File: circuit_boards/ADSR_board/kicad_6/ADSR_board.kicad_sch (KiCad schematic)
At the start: 14 parts, among them J1 ribbon_port, J2 modosc_port, J3 VCO_port, J4 VCF_port, U101 TL072

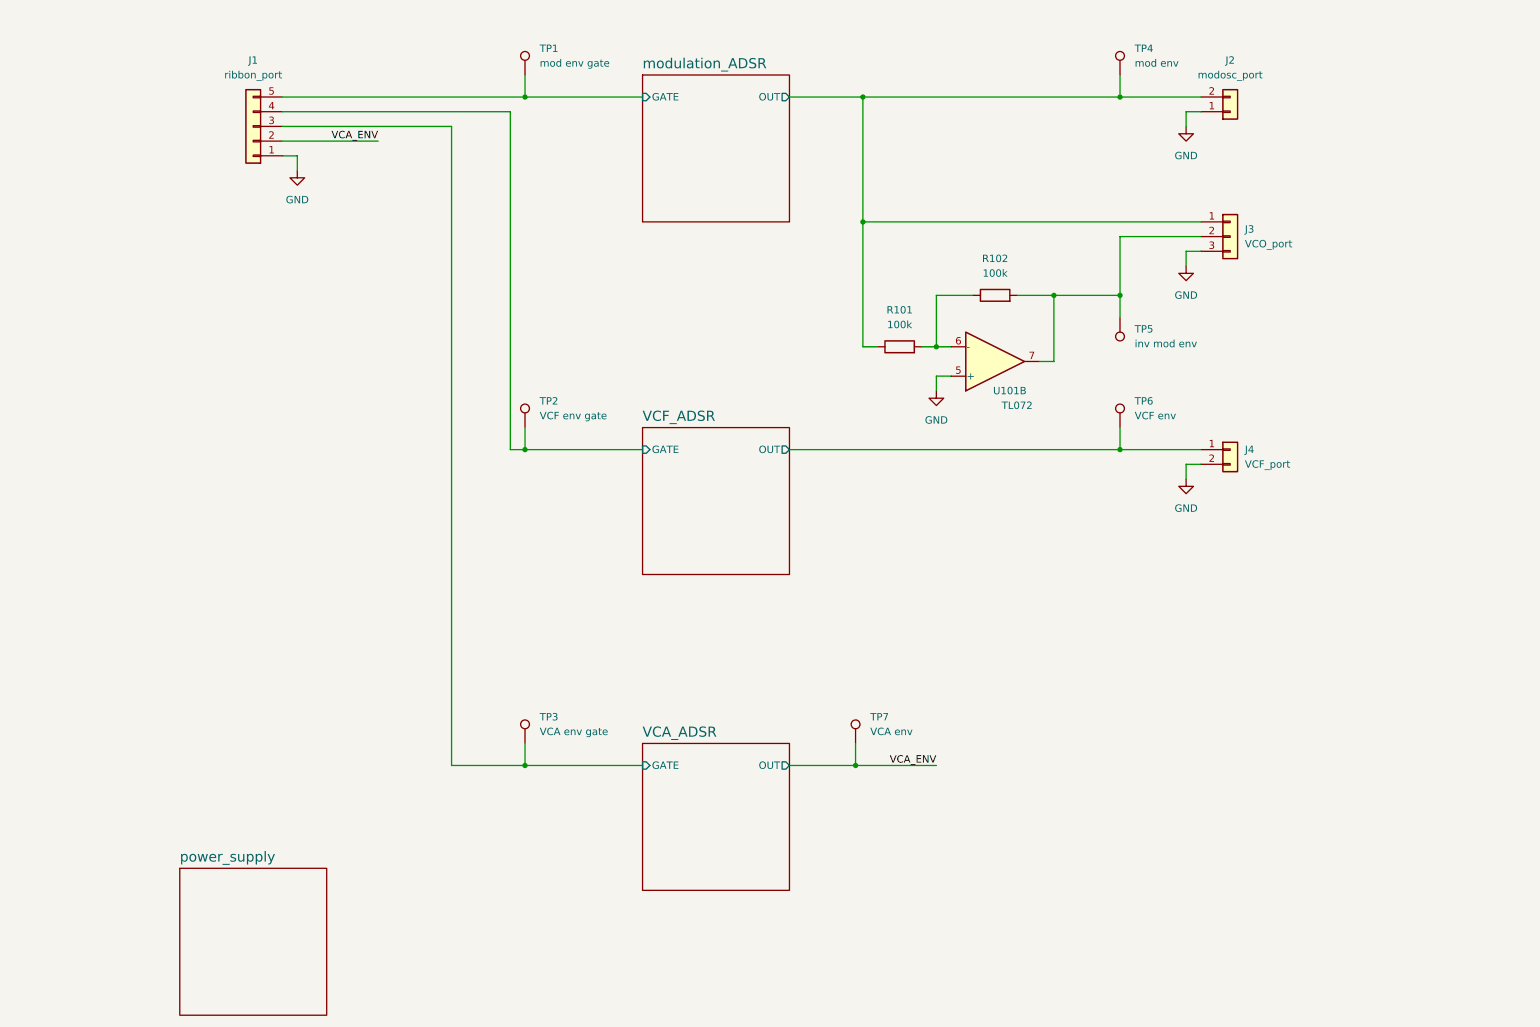
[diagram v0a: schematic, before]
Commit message: Upgrade ADSR to analog swiitch version
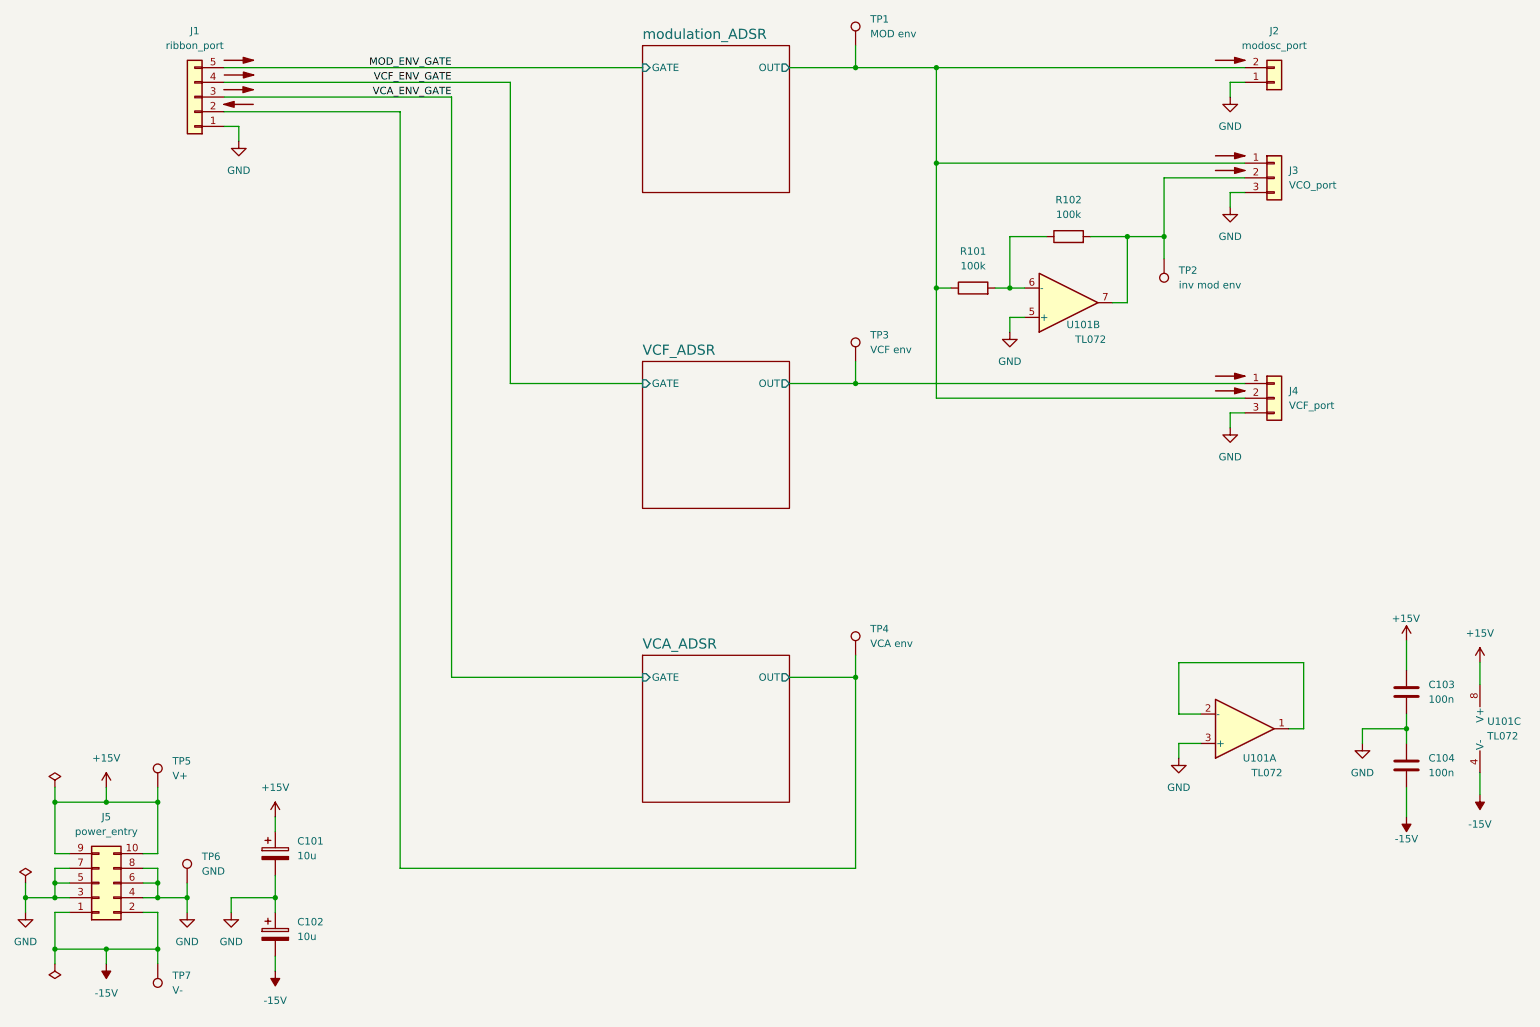
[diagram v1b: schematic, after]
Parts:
- removed J4: VCF_port, Connector_Molex:Molex_KK-254_AE-6410-02A_1x02_P2.54mm_Vertical, symbol Connector_Generic:Conn_01x02
- removed TP1: mod env gate, TestPoint:TestPoint_Keystone_5000-5004_Miniature, symbol Connector:TestPoint
- removed TP2: VCF env gate, TestPoint:TestPoint_Keystone_5000-5004_Miniature, symbol Connector:TestPoint
- removed TP3: VCA env gate, TestPoint:TestPoint_Keystone_5000-5004_Miniature, symbol Connector:TestPoint
- added C101, C102: 10u, Capacitor_THT:CP_Radial_D6.3mm_P2.50mm, symbol Device:C_Polarized
- added C103, C104: 100n, Capacitor_SMD:C_0805_2012Metric, symbol Device:C
- added J4: VCF_port, Connector_Molex:Molex_KK-254_AE-6410-03A_1x03_P2.54mm_Vertical, symbol Connector_Generic:Conn_01x03
- added J5: power_entry, Connector_IDC:IDC-Header_2x05_P2.54mm_Vertical, symbol Connector_Generic:Conn_02x05_Odd_Even
- added TP5: V+, TestPoint:TestPoint_Keystone_5000-5004_Miniature, symbol Connector:TestPoint
- added TP6: GND, TestPoint:TestPoint_Bridge_Pitch7.62mm_Drill1.3mm, symbol Connector:TestPoint
- added TP7: V-, TestPoint:TestPoint_Keystone_5000-5004_Miniature, symbol Connector:TestPoint
- added unit 3 of U101
- added unit 2 of U101
- TP1: renamed from TP4; value mod env -> MOD env
- U101: footprint Package_SO:SO-8_5.3x6.2mm_P1.27mm -> Package_SO:SOIC-8_3.9x4.9mm_P1.27mm
- renumbered TP5 to TP2, TP6 to TP3, TP7 to TP4
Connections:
- net GND: now also U101.3 (+), C101.2, C102.1, C103.2, C104.1, J4.3 (Pin_3), J5.3 (Pin_3), J5.4 (Pin_4), J5.5 (Pin_5), J5.6 (Pin_6), J5.7 (Pin_7), J5.8 (Pin_8), TP6.1, U101.5 (+); no longer U101.5 (+)
- net VCF_ADSR/OUT: now also J4.1 (Pin_1)
- net modulation_ADSR/OUT: now also J4.2 (Pin_2)
- net at R101.2, R102.1: now also U101.6 (-); no longer U101.6 (-)
- net at J3.2 (Pin_2), R102.2, TP2.1: now also U101.7; no longer U101.7
- net VCA_ADSR/GATE renamed VCA_ENV_GATE
- net VCA_ENV renamed VCA_ADSR/OUT
- net VCF_ADSR/GATE renamed VCF_ENV_GATE
- net modulation_ADSR/GATE renamed MOD_ENV_GATE
- new net: U101.1, U101.2 (-)
- new net +15V: C101.1, C103.1, J5.10 (Pin_10), J5.9 (Pin_9), TP5.1, U101.8 (V+)
- new net -15V: C102.2, C104.2, J5.1 (Pin_1), J5.2 (Pin_2), TP7.1, U101.4 (V-)
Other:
- removed sheet power_supply
- moved on the sheet: J1, J2, J3, R101, R102, TP1, TP2, TP3, TP4, U101A
